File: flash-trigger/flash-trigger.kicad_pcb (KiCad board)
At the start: 2 copper layers, 22 x 32 mm, 32 parts, among them J1 TRIG, J2 GND, Q1 NDS331N, SW1 PCM12, SW2 Bat Test, U1 74LV123, U2 BD48K27G

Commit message: Fixes and improvements
 * fix the preflash detection
 * clean the canon hot shoe schematics up
 * enlarge the hotshoe pcb and place two new mounting pins
 * change the battery low to a battery good detection
 * move the supervisor ic away from the hot shoe rail
 * use a longer pogo pin
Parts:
- added J3: GND, Connector_MillMax:0508_20mil, B.Cu at (88.5, 75.2)
- added J4: GND, Connector_MillMax:0508_20mil, B.Cu at (73.5, 75.2)
- D6: value RED -> GREEN
- U2: value BD48K27G -> BD49KxxG
- moved R13 2.12 mm to (81.8, 64.2), turned to 0 degrees
- moved R5 1.49 mm to (81.8, 62.7), turned to 0 degrees
- moved U2 1.21 mm to (77.4, 63.0)
- moved R6 0.10 mm to (77.0, 74.6)
- moved D6 0.05 mm to (83.6, 55.1)
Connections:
- D6 pad 1: Net-(D6-Pad1) -> GND
- D6 pad 2: +3V0 -> Net-(D6-Pad2)
- R11 pad 1: Net-(D6-Pad1) -> Net-(D6-Pad2)
- U1 pad 1: /TRIG -> GND
- U1 pad 2: +3V0 -> /TRIG
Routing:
- net GND: track 13.4 -> 27.8 mm, vias 15 -> 11
- net Net-(D6-Pad2): track 0.00 -> 11.0 mm, vias 0 -> 1
- net Net-(D6-Pad1): track 9.61 -> 0.00 mm, vias 1 -> 0
- net +3V0: track 77.3 -> 83.9 mm, vias 0 -> 1
- net Net-(R13-Pad1): track 10.5 -> 8.77 mm
- net Net-(Q1-Pad1): track 7.68 -> 8.63 mm
- net /TRIG: track 34.4 -> 35.1 mm

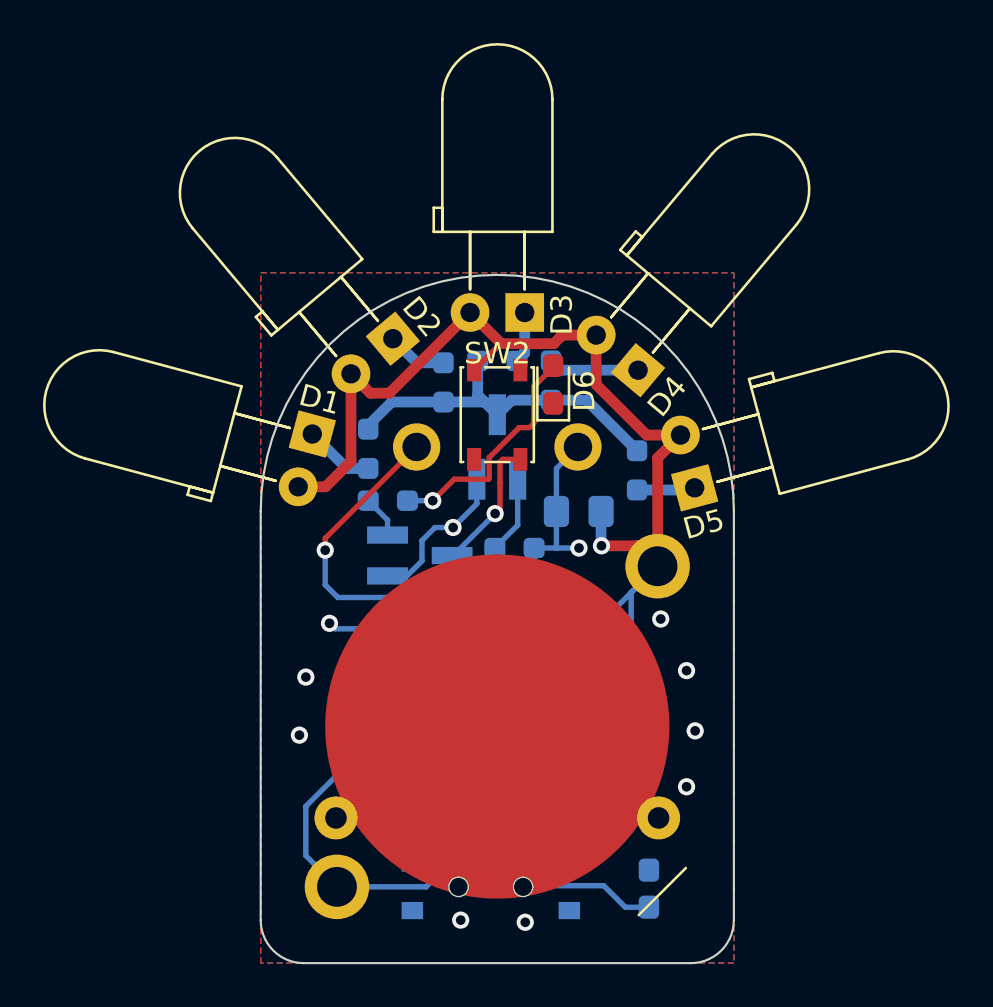
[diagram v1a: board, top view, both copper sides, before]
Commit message: flash-trigger: Drop RC circuit and improve layout
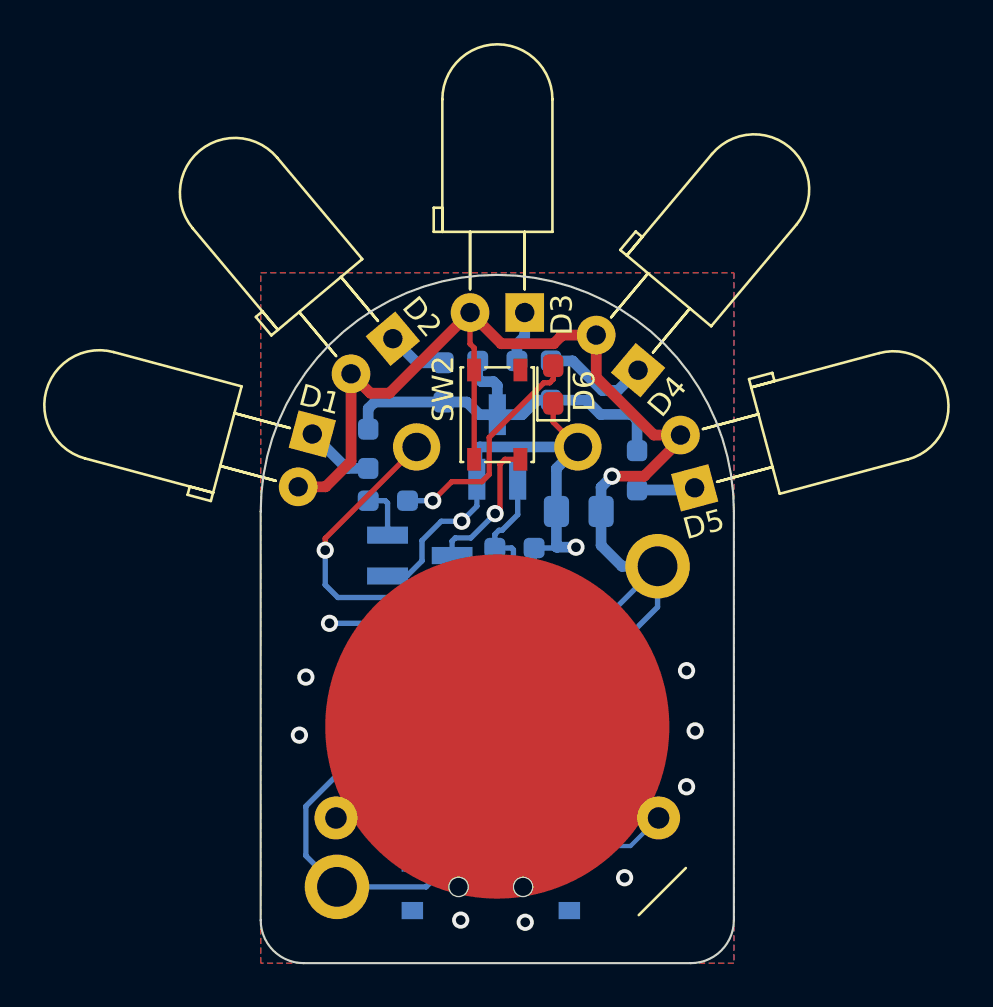
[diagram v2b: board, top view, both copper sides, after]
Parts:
- removed C5: 2.2n, Capacitor_SMD:C_0603_1608Metric_Pad1.08x0.95mm_HandSolder
- removed R12: 1k5, Resistor_SMD:R_0603_1608Metric_Pad0.98x0.95mm_HandSolder
- moved C2 0.06 mm to (85.3, 74.6), turned to 180 degrees
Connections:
- SW1 pad 1: /PREFLASH_DELAYED -> /PREFLASH
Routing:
- net GND: track 27.8 -> 43.1 mm
- net /PREFLASH_DELAYED: track 10.6 -> 0.00 mm
- net +3V0: track 83.9 -> 91.0 mm
- net Net-(Q1-Pad3): track 16.7 -> 19.1 mm
- net /PREFLASH: track 4.92 -> 6.99 mm
- net Net-(C1-Pad2): track 6.32 -> 7.44 mm
- net Net-(R13-Pad1): track 8.77 -> 9.73 mm
- net Net-(Q1-Pad1): track 8.63 -> 9.57 mm
- net Net-(D4-Pad1): track 4.22 -> 5.00 mm
- net Net-(SW1-Pad2): track 10.1 -> 10.9 mm
- net /TRIG: track 35.1 -> 35.7 mm
- net Net-(D6-Pad2): track 11.0 -> 10.5 mm

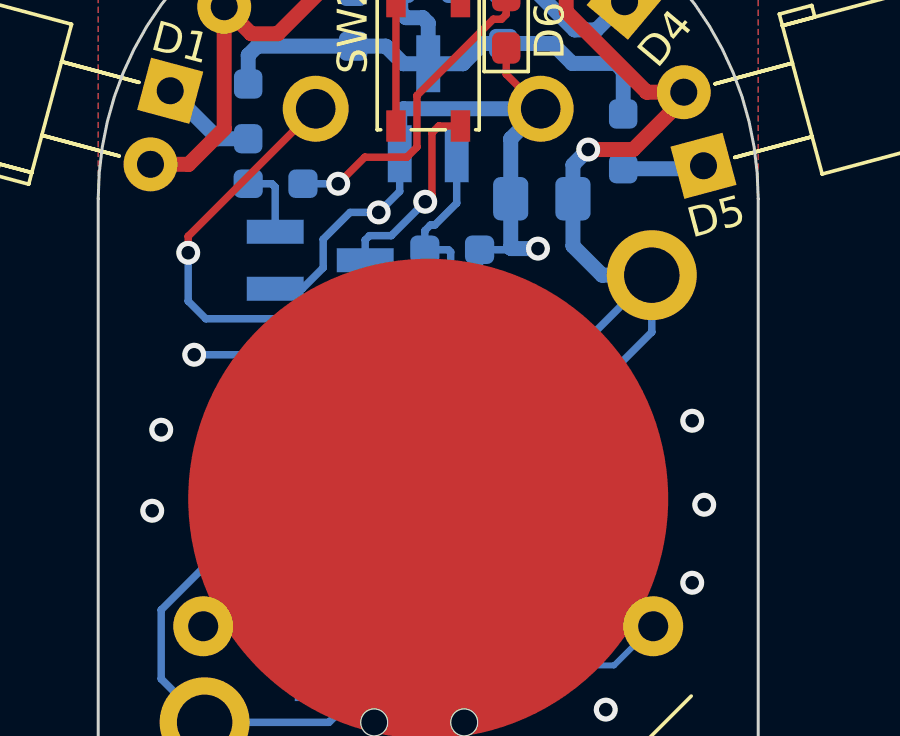
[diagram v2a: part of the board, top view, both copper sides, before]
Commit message: Renumber RefDes and add OSHW logo and URL
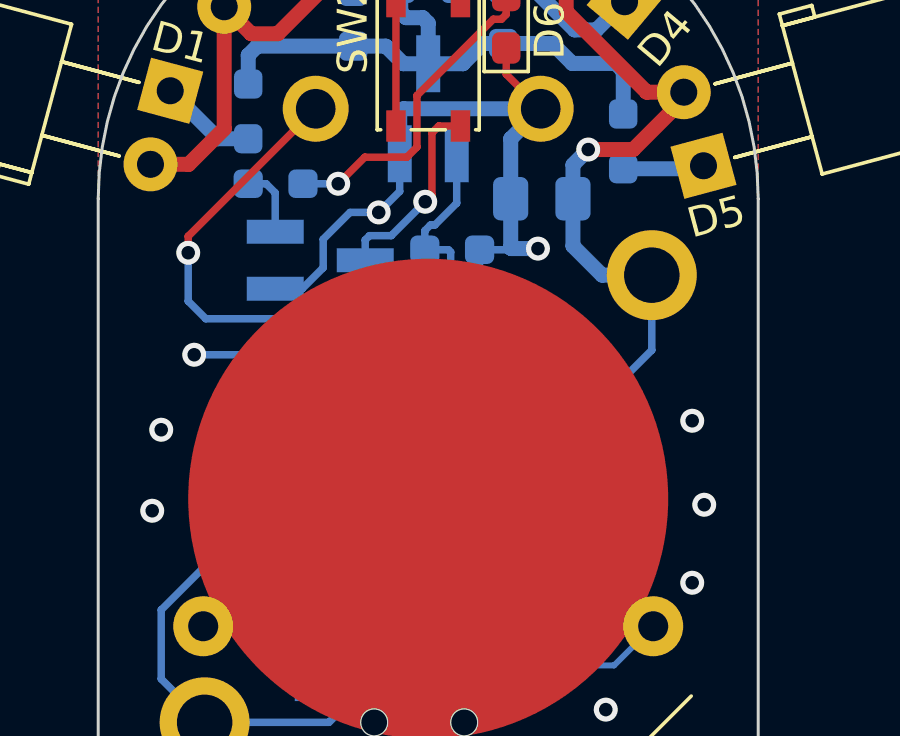
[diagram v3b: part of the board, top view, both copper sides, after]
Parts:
- renumbered C2 to C1, C3 to C2, C4 to C3, C1 to C4, R3 to R10, R13 to R12, R7 to R3, R8 to R4, R9 to R5, R4 to R6, R5 to R7, R6 to R8, R10 to R9
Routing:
- net +3V0: track 91.0 -> 88.3 mm

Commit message: flash-trigger: replace BD49KxxG with BD49K27G
We use a 2.7V voltage supervisor.
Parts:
- U2: value BD49KxxG -> BD49K27G
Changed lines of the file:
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@@
       (effects (font (size 1 1) (thickness 0.15)) (justify mirror))
     )
-    (fp_text value "BD49KxxG" (at 0 -2.5 180) (layer "B.Fab")
+    (fp_text value "BD49K27G" (at 0 -2.5 180) (layer "B.Fab")
       (effects (font (size 1 1) (thickness 0.15)) (justify mirror))
     )

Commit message: flash-trigger: Increase C2 to 100uF
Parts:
- C2: value 47u -> 100u
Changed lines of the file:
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@@
       (effects (font (size 1 1) (thickness 0.15)) (justify mirror))
     )
-    (fp_text value "47u" (at 0 -1.68) (layer "B.Fab")
+    (fp_text value "100u" (at 0 -1.68) (layer "B.Fab")
       (effects (font (size 1 1) (thickness 0.15)) (justify mirror))
     )

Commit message: flash-trigger: Update value of SW2
Reflect the actual component value instead of its function.
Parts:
- SW2: value Bat Test -> PTS810
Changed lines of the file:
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@@
       (effects (font (size 1 1) (thickness 0.15)))
     )
-    (fp_text value "Bat Test" (at 0 2.6 90) (layer "F.Fab")
+    (fp_text value "PTS810" (at 0 2.6 90) (layer "F.Fab")
       (effects (font (size 1 1) (thickness 0.15)))
     )
